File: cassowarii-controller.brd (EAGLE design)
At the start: 34.3 x 26.7 mm, 18 parts, among them J1 2-PIN_2MM-H, J2 2-PIN_2MM-H, J3 AVR_SPI_PROG_3X2PTH, J4 Power, U1 ATTiny85

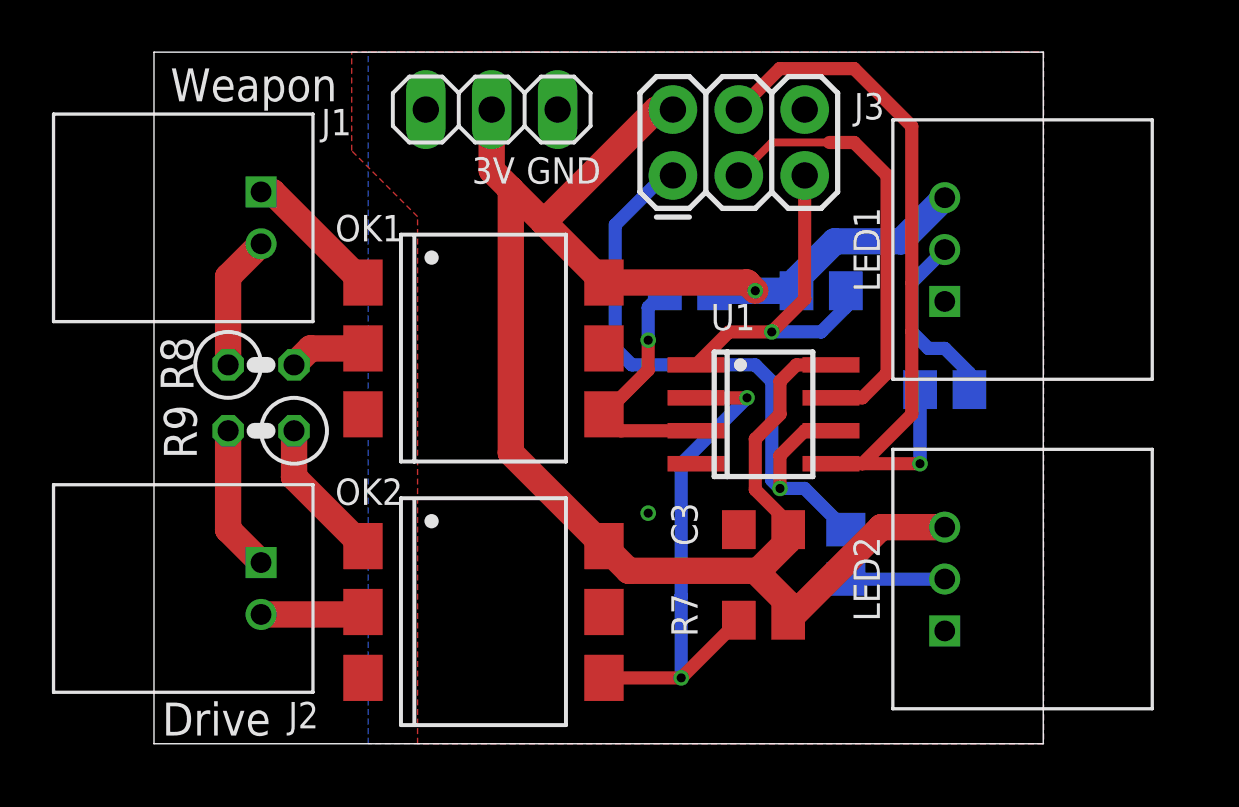
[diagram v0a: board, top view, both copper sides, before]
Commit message: Replace optoisolator
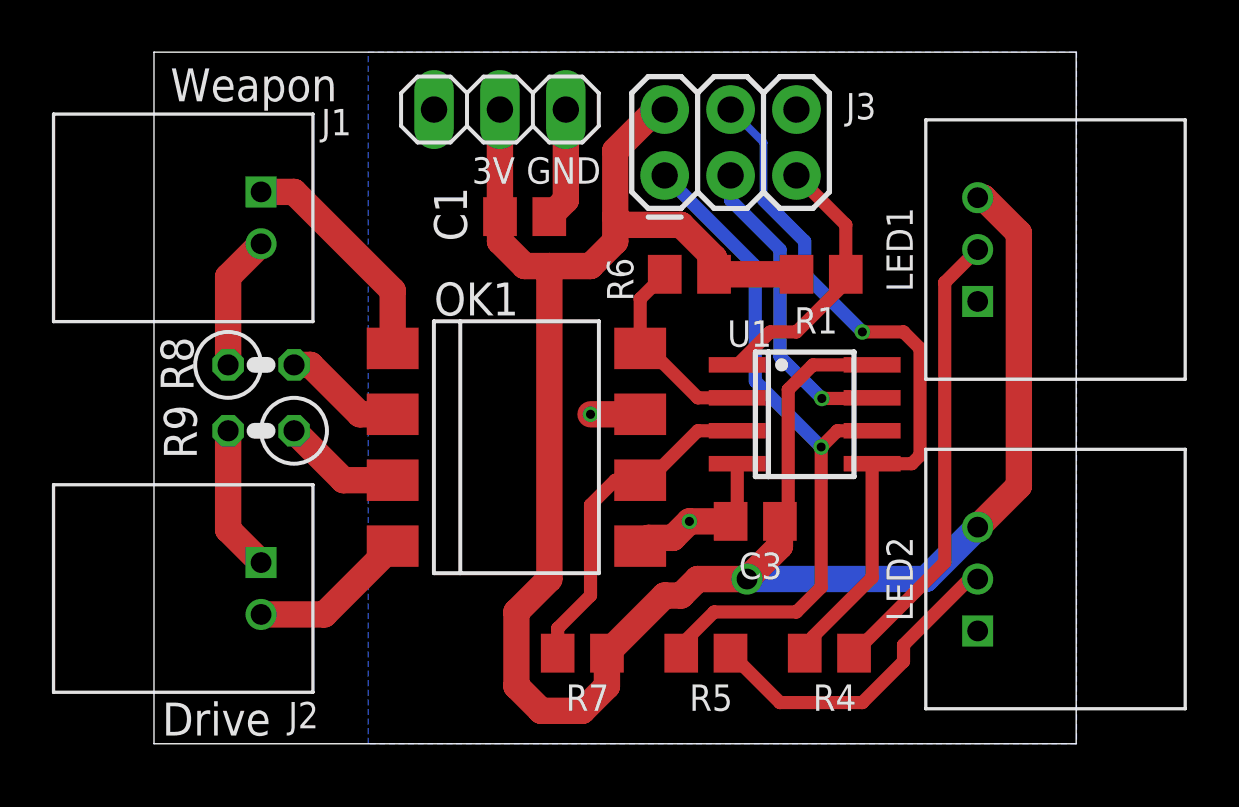
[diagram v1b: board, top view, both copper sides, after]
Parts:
- removed OK2: H11L1MS, optocoupler:DIL6-SMD
- added C1: 22uF, resistor:C0805
- OK1: value H11L1MS -> LTV826S; device optocoupler:DIL6-SMD -> optocoupler:DIL8-SMD
- R6, R7: value 270 -> 10k
- moved R4 11.1 mm to (26.0, 3.49), flipped to the top, turned to 0 degrees
- moved R7 7.10 mm to (16.5, 3.49)
- moved R5 6.61 mm to (21.3, 3.49), flipped to the top, turned to 0 degrees
- moved OK1 4.02 mm to (14.0, 11.4)
- moved U1 1.59 mm to (25.1, 12.7)
- moved LED1 1.27 mm to (31.8, 19.1)
- moved LED2 1.27 mm to (31.8, 6.35)
- moved R1 0.64 mm to (25.7, 18.1), flipped to the top, turned to 180 degrees
- moved R6 0.64 mm to (20.6, 18.1), flipped to the top, turned to 0 degrees
- moved C3 0.45 mm to (23.2, 8.57)
- moved J3 0.32 mm to (19.7, 21.9)
- moved J4 0.32 mm to (13.3, 24.4)
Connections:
- removed net N$10: OK2.1, R9.1
- new net N$5: OK1.3, R9.1
- net GND: now also C1.2, OK1.7; no longer OK2.5
- net N$6: now also OK1.4; no longer OK2.2
- net PB3: now also OK1.8, R6.1; no longer OK2.4, R7.1
- net PB4: now also OK1.6, R7.1; no longer OK1.4, R6.1
- net VCC: now also C1.1; no longer OK1.6, OK2.6
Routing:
- net VCC: track 74.3 -> 89.0 mm
- net GND: track 0.00 -> 12.5 mm, vias 1 -> 2
- net PB3: track 19.9 -> 7.78 mm, vias 2 -> 0
- net N$1: track 7.22 -> 17.5 mm
- net N$2: track 3.81 -> 12.7 mm
- net N$10: track 5.55 -> 0.00 mm
- net PB2: track 16.9 -> 12.0 mm, vias 0 -> 1
- net N$5: track 0.00 -> 4.59 mm
- net PB4: track 9.55 -> 13.1 mm, vias 1 -> 0
- net N$7: track 5.37 -> 8.88 mm
- net RESET: track 13.9 -> 10.4 mm, vias 1 -> 0
- net N$6: track 3.97 -> 6.16 mm
- net LED1: track 25.4 -> 27.2 mm
- net N$8: track 2.92 -> 4.59 mm
- net LED2: track 28.3 -> 27.6 mm
- removed copper zone on layer 1, net GND
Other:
- board size 34.3 x 26.7 mm -> 35.5 x 26.7 mm
